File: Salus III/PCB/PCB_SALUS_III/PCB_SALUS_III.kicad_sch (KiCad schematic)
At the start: 42 parts, among them J1 Conn_01x02_Pin, J2 Conn_01x01_Pin, J3 Conn_01x01_Pin, J4 Conn_01x02_Pin, J5 Conn_01x02_Pin, J6 Conn_01x02_Pin, J7 Conn_01x02_Pin, K1 Relay_SPDT, Q1 IRF4905, Q2 IRF4905, Q3 IRF4905, Q4 IRF4905, Q5 IRLB8721PBF, Q6 IRLB8721PBF, Q7 IRLB8721PBF, Q8 IRLB8721PBF, Q9 IRLB8721PBF, U1 ESP32-DEVKITC-32D, U2 RASPBERRY_PI_4B_4GB

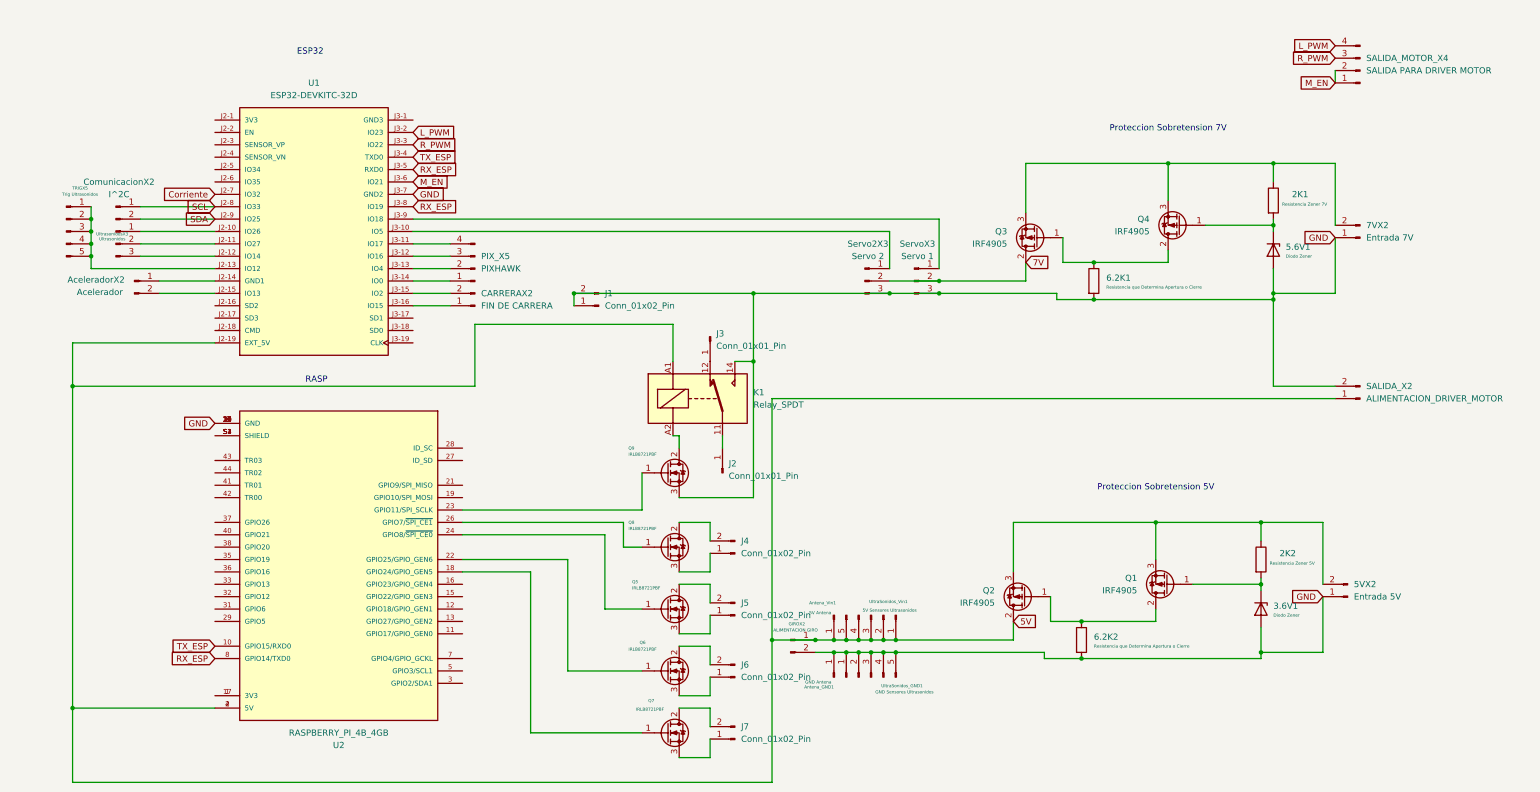
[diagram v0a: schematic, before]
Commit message: Se agregaron Modificaciones de PCB. Queda modificar raspy por tira de pines
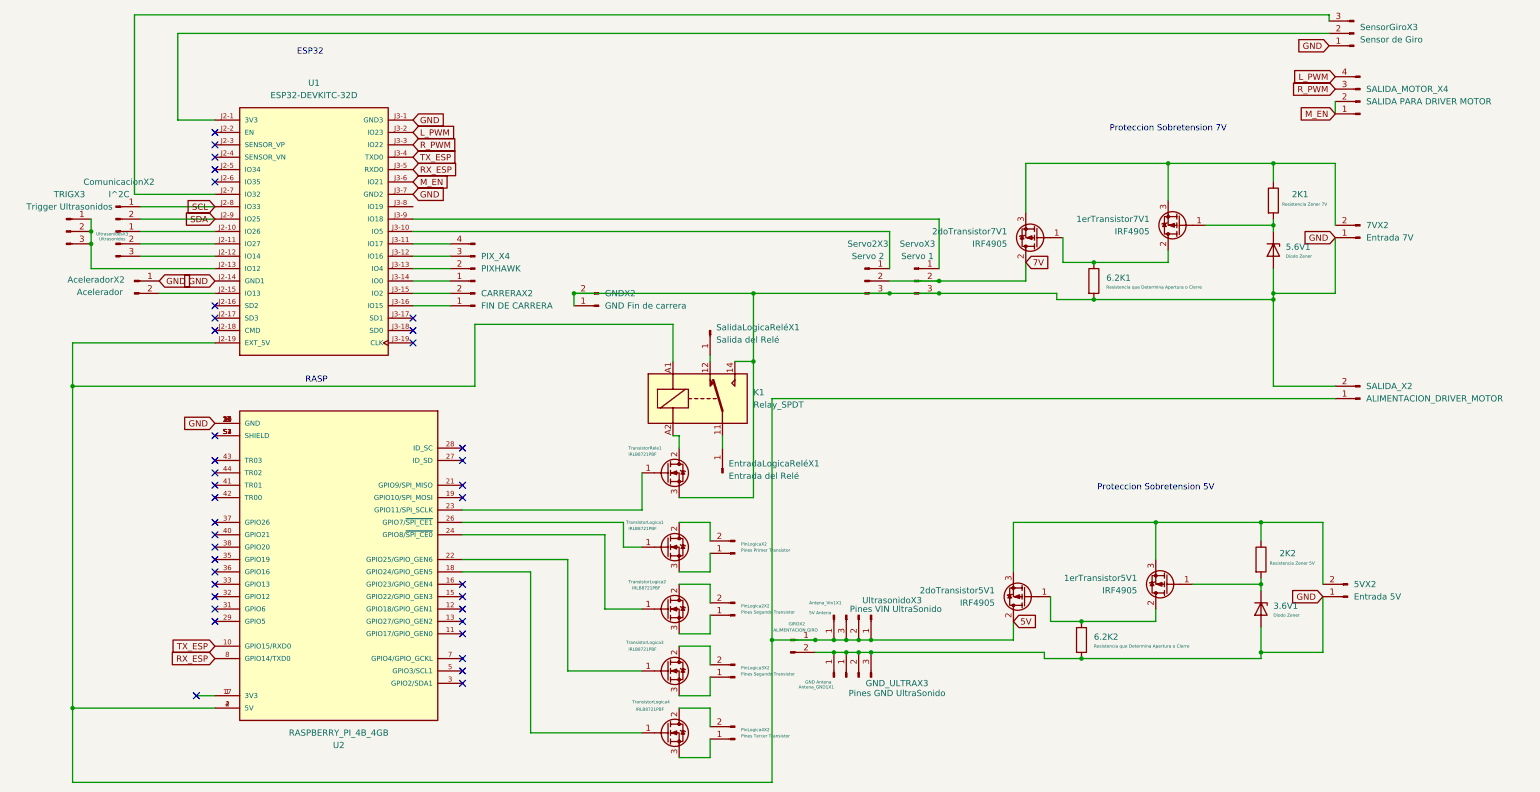
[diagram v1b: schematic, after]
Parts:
- removed TRIGX5: Trig Ultrasonidos, symbol Connector:Conn_01x05_Pin
- removed UltraSonidos_GND1: GND Sensores Ultrasonidos, symbol Connector:Conn_01x05_Pin
- removed UltraSonidos_Vin1: 5V Sensores Ultrasonidos, symbol Connector:Conn_01x05_Pin
- added GND_ULTRAX3: Pines GND UltraSonido, Connector_PinHeader_2.54mm:PinHeader_1x03_P2.54mm_Vertical, symbol Connector:Conn_01x03_Pin
- added SensorGiroX3: Sensor de Giro, Connector_PinHeader_2.54mm:PinHeader_1x03_P2.54mm_Vertical, symbol Connector:Conn_01x03_Pin
- added TRIGX3: Trigger Ultrasonidos, Connector_PinHeader_2.54mm:PinHeader_1x03_P2.54mm_Vertical, symbol Connector:Conn_01x03_Pin
- added UltrasonidoX3: Pines VIN UltraSonido, Connector_PinHeader_2.54mm:PinHeader_1x03_P2.54mm_Vertical, symbol Connector:Conn_01x03_Pin
- 2K1, 2K2, 6.2K1, 6.2K2: footprint (none) -> Resistor_THT:R_Axial_DIN0207_L6.3mm_D2.5mm_P10.16mm_Horizontal
- 3.6V1, 5.6V1: footprint (none) -> Diode_THT:D_DO-41_SOD81_P12.70mm_Horizontal
- 5VX2, 7VX2, AceleradorX2, CARRERAX2, ComunicacionX2, GIROX2, SALIDA_X2: footprint (none) -> Connector_PinHeader_2.54mm:PinHeader_1x02_P2.54mm_Vertical
- Antena_GND1X1: renamed from Antena_GND1; footprint (none) -> Connector_PinHeader_2.54mm:PinHeader_1x01_P2.54mm_Vertical
- Antena_Vin1X1: renamed from Antena_Vin1; footprint (none) -> Connector_PinHeader_2.54mm:PinHeader_1x01_P2.54mm_Vertical
- EntradaLogicaReléX1: renamed from J2; value Conn_01x01_Pin -> Entrada del Relé; footprint (none) -> Connector_PinHeader_2.54mm:PinHeader_1x01_P2.54mm_Vertical
- GNDX2: renamed from J1; value Conn_01x02_Pin -> GND Fin de carrera; footprint (none) -> Connector_PinHeader_2.54mm:PinHeader_1x02_P2.54mm_Vertical
- K1: footprint (none) -> Relay_THT:Relay_SPDT_Finder_36.11
- PIX_X4: renamed from PIX_X5; footprint (none) -> Connector_PinSocket_2.54mm:PinSocket_1x04_P2.54mm_Vertical
- PinLogica2X2: renamed from J5; value Conn_01x02_Pin -> Pines Segundo Transistor; footprint (none) -> Connector_PinHeader_2.54mm:PinHeader_1x02_P2.54mm_Vertical
- PinLogica3X2: renamed from J6; value Conn_01x02_Pin -> Pines Segundo Transistor; footprint (none) -> Connector_PinHeader_2.54mm:PinHeader_1x02_P2.54mm_Vertical
- PinLogica4X2: renamed from J7; value Conn_01x02_Pin -> Pines Tercer Transistor; footprint (none) -> Connector_PinHeader_2.54mm:PinHeader_1x02_P2.54mm_Vertical
- PinLogicaX2: renamed from J4; value Conn_01x02_Pin -> Pines Primer Transistor; footprint (none) -> Connector_PinHeader_2.54mm:PinHeader_1x02_P2.54mm_Vertical
- SALIDA_MOTOR_X4: footprint (none) -> Connector_PinHeader_2.54mm:PinHeader_1x04_P2.54mm_Vertical
- SalidaLogicaReléX1: renamed from J3; value Conn_01x01_Pin -> Salida del Relé; footprint (none) -> Connector_PinHeader_2.54mm:PinHeader_1x01_P2.54mm_Vertical
- Servo2X3, ServoX3, UltrasonidosX3: footprint (none) -> Connector_PinHeader_2.54mm:PinHeader_1x03_P2.54mm_Vertical
- U1: footprint ESP32-DEVKITC-32D:MODULE_ESP32-DEVKITC-32D -> Huella ESP:MODULE_ESP32-DEVKITC-32D
- U2: footprint RASPBERRY_PI_4B_4GB:MODULE_RASPBERRY_PI_4B_4GB -> Huella_Rasp:MODULE_RASPBERRY_PI_4B_4GB
- renumbered Q1 to 1erTransistor5V1, Q4 to 1erTransistor7V1, Q2 to 2doTransistor5V1, Q3 to 2doTransistor7V1, Q8 to TransistorLogica1, Q5 to TransistorLogica2, Q6 to TransistorLogica3, Q7 to TransistorLogica4, Q9 to TransistorRele1
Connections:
- net 5V: now also UltrasonidoX3.1 (Pin_1), UltrasonidoX3.2 (Pin_2), UltrasonidoX3.3 (Pin_3)
- net GND: now also AceleradorX2.1 (Pin_1), U1.J2-14 (GND1), U1.J3-1 (GND3), GND_ULTRAX3.1 (Pin_1), GND_ULTRAX3.2 (Pin_2), GND_ULTRAX3.3 (Pin_3), SensorGiroX3.1 (Pin_1)
- net RX_ESP: no longer U1.J3-8 (IO19)
- net at U1.J2-1 (3V3): now also SensorGiroX3.2 (Pin_2)
- net at U1.J2-13 (IO12): now also TRIGX3.1 (Pin_1), TRIGX3.2 (Pin_2), TRIGX3.3 (Pin_3)
- net Corriente: no longer names the net of U1.J2-7 (IO32)
- net Corriente: now also SensorGiroX3.3 (Pin_3)
- no-connect marks 0 -> 38
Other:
- moved on the sheet: SALIDA_MOTOR_X4, SalidaLogicaReléX1

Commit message: Parece ser la PCB definitiva de SALUS III por lo menos parte logica
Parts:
- removed U2: RASPBERRY_PI_4B_4GB, Huella_Rasp:MODULE_RASPBERRY_PI_4B_4GB, symbol RASPBERRY_PI_4B_4GB:RASPBERRY_PI_4B_4GB
- added 47K1: Resistencia Base 5V, Resistor_THT:R_Axial_DIN0207_L6.3mm_D2.5mm_P10.16mm_Horizontal, symbol Device:R
- added 47K2: Resistencia Base 7V, Resistor_THT:R_Axial_DIN0207_L6.3mm_D2.5mm_P10.16mm_Horizontal, symbol Device:R
- added J1, J2: Conn_01x20_Pin, Connector_PinHeader_2.54mm:PinHeader_1x20_P2.54mm_Vertical, symbol Connector:Conn_01x20_Pin
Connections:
- net 5V: now also J2.1 (Pin_1)
- net GND: now also J1.1 (Pin_1), J1.16 (Pin_16), J2.10 (Pin_10), J2.15 (Pin_15), J2.17 (Pin_17), J2.3 (Pin_3), J2.7 (Pin_7)
- net L_PWM: now also U1.J3-3 (IO22); no longer U1.J3-2 (IO23)
- net RX_ESP: now also J2.5 (Pin_5)
- net R_PWM: now also U1.J3-2 (IO23); no longer U1.J3-3 (IO22)
- net TX_ESP: now also J2.4 (Pin_4)
- net at TransistorLogica1.1 (G): now also J2.11 (Pin_11)
- net at TransistorLogica4.1 (G): now also J2.16 (Pin_16)
- net at TransistorLogica3.1 (G): now also J2.13 (Pin_13)
- net at TransistorRele1.1 (G): now also J2.9 (Pin_9)
- net at TransistorLogica2.1 (G): now also J2.12 (Pin_12)
- net at 2K1.2, 5.6V1.1 (K): now also 47K2.1; no longer 1erTransistor7V1.1 (G)
- net at 2K2.2, 3.6V1.1 (K): now also 47K1.1; no longer 1erTransistor5V1.1 (G)
- new net: 1erTransistor7V1.1 (G), 47K2.2
- new net: 1erTransistor5V1.1 (G), 47K1.2
- no-connect marks 38 -> 36
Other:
- note added: "3V"
- note added: "3V3"
- note added: "5V"
- note added: "GND"
- note added: "Gpio 0"
- note added: "Gpio 1"
- note added: "Gpio 10"
- note added: "Gpio 11"
- note added: "Gpio 12"
- note added: "Gpio 13"
- note added: "Gpio 14 (TX)"
- note added: "Gpio 15 (RX)"
- note added: "Gpio 16"
- note added: "Gpio 17"
- note added: "Gpio 18"
- note added: "Gpio 19"
- note added: "Gpio 2 SDA"
- note added: "Gpio 20"
- note added: "Gpio 21"
- note added: "Gpio 22"
- note added: "Gpio 23"
- note added: "Gpio 24"
- note added: "Gpio 25"
- note added: "Gpio 26"
- note added: "Gpio 27"
- note added: "Gpio 3 SCL"
- note added: "Gpio 4"
- note added: "Gpio 5"
- note added: "Gpio 6"
- note added: "Gpio 7"
- note added: "Gpio 8"
- note added: "Gpio 9"

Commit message: se agrego el diodo TVS a probar para proteger de cierres de Relé
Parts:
- added D1: 1N62xxA, Diode_THT:D_DO-201AE_P15.24mm_Horizontal, symbol Diode:1N62xxA
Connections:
- net GND: now also D1.2 (A2)
- net at K1.A2, TransistorRele1.2 (D): now also D1.1 (A1)
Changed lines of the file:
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@@
 	)
 	(junction
+		(at 139.7 109.22)
+		(diameter 0)
+		(color 0 0 0 0)
+	)
+	(junction
 		(at 173.99 152.4)
 		(diameter 0)
@@
 	(wire
 		(pts
-			(xy 139.7 107.95) (xy 139.7 110.49)
+			(xy 139.7 148.59) (xy 146.05 148.59)
 		)
 		(stroke
@@
 	(wire
 		(pts
-			(xy 139.7 148.59) (xy 146.05 148.59)
+			(xy 44.45 73.66) (xy 19.05 73.66)
 		)
 		(stroke
@@
 	(wire
 		(pts
-			(xy 44.45 73.66) (xy 19.05 73.66)
+			(xy 19.05 68.58) (xy 19.05 73.66)
 		)
 		(stroke
@@
 	(wire
 		(pts
-			(xy 19.05 68.58) (xy 19.05 73.66)
+			(xy 102.87 156.21) (xy 132.08 156.21)
 		)
 		(stroke
@@
 	(wire
 		(pts
-			(xy 102.87 156.21) (xy 132.08 156.21)
+			(xy 69.85 142.24) (xy 102.87 142.24)
 		)
 		(stroke
@@
 	(wire
 		(pts
-			(xy 69.85 142.24) (xy 102.87 142.24)
+			(xy 139.7 107.95) (xy 139.7 109.22)
 		)
 		(stroke
@@
 	(wire
 		(pts
+			(xy 80.01 116.84) (xy 69.85 116.84)
+		)
+		(stroke
+			(width 0)
+			(type default)
+		)
+	)
+	(wire
+		(pts
 			(xy 151.13 92.71) (xy 154.94 92.71)
 		)
@@
 	(wire
 		(pts
+			(xy 80.01 109.22) (xy 80.01 116.84)
+		)
+		(stroke
+			(width 0)
+			(type default)
+		)
+	)
+	(wire
+		(pts
 			(xy 176.53 152.4) (xy 179.07 152.4)
 		)
@@
 	(wire
 		(pts
+			(xy 132.08 109.22) (xy 80.01 109.22)
+		)
+		(stroke
+			(width 0)
+			(type default)
+		)
+	)
+	(wire
+		(pts
 			(xy 261.62 64.77) (xy 261.62 66.04)
 		)
@@
 	(wire
 		(pts
+			(xy 139.7 109.22) (xy 139.7 110.49)
+		)
+		(stroke
+			(width 0)
+			(type default)
+		)
+	)
+	(wire
+		(pts
 			(xy 210.82 62.23) (xy 210.82 52.07)
 		)
@@
 					(unit 1)
 				)
+			)
+		)
+	)
+	(symbol
+		(lib_id "Diode:1N62xxA")
+		(at 135.89 109.22 180)
+		(unit 1)
+		(exclude_from_sim no)
+		(in_bom yes)
+		(on_board yes)
+		(dnp no)
+		(fields_autoplaced yes)
+		(property "Reference" "D1"
+			(at 135.89 102.87 0)
+			(effects
+				(font
+					(size 1.27 1.27)
+				)
+			)
+		)
+		(property "Value" "1N62xxA"
+			(at 135.89 105.41 0)
+			(effects
+				(font
+					(size 1.27 1.27)
+				)
+			)
+		)
+		(property "Footprint" "Diode_THT:D_DO-201AE_P15.24mm_Horizontal"
+			(at 135.89 104.14 0)
+			(effects
+				(font
+					(size 1.27 1.27)
+				)
+				(hide yes)
+			)
+		)
+		(property "Datasheet" "https://www.vishay.com/docs/88301/15ke.pdf"
+			(at 137.16 109.22 0)
+			(effects
+				(font
+					(size 1.27 1.27)
+				)
+				(hide yes)
+			)
+		)
+		(property "Description" "1500W unidirectional TRANSZORB® Transient Voltage Suppressor, DO-201AE"
+			(at 135.89 109.22 0)
+			(effects
+				(font
+					(size 1.27 1.27)
+				)
+				(hide yes)
+			)
+		)
+		(pin "2"
+		)
+		(pin "1"
+		)
+		(instances
+			(project ""
+				(path "/3613b1f1-6164-4a03-ab5f-c520c1df4874"
+					(reference "D1")
+					(unit 1)
+				)

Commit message: Cambios para realizarla en acido preparados
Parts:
- D1: footprint Diode_THT:D_DO-201AE_P15.24mm_Horizontal -> Diode_THT:D_DO-201AE_P12.70mm_Horizontal
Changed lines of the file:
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@@
 			)
 		)
-		(property "Footprint" "Diode_THT:D_DO-201AE_P15.24mm_Horizontal"
+		(property "Footprint" "Diode_THT:D_DO-201AE_P12.70mm_Horizontal"
 			(at 135.89 104.14 0)
 			(effects

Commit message: no se que cambio
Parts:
- removed SensorGiroX3: Sensor de Giro, Connector_PinHeader_2.54mm:PinHeader_1x03_P2.54mm_Vertical, symbol Connector:Conn_01x03_Pin
- added Giro1: Conn_01x02_Pin, Connector_PinHeader_2.54mm:PinHeader_1x02_P2.54mm_Vertical, symbol Connector:Conn_01x02_Pin
- added Pan1, PinesAnalogicos1, SensorCorriente1, Tilt1: Conn_01x03_Pin, Connector_PinHeader_2.54mm:PinHeader_1x03_P2.54mm_Vertical, symbol Connector:Conn_01x03_Pin
- added SensorTemperatura1: Conn_01x04_Pin, Connector_PinHeader_2.54mm:PinHeader_1x04_P2.54mm_Vertical, symbol Connector:Conn_01x04_Pin
- D1: footprint Diode_THT:D_DO-201AE_P12.70mm_Horizontal -> Diode_THT:D_DO-201AE_P15.24mm_Horizontal
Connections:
- net 5V: now also Giro1.2 (Pin_2), Pan1.2 (Pin_2), SensorTemperatura1.4 (Pin_4), Tilt1.2 (Pin_2)
- net GND: now also Giro1.1 (Pin_1), Pan1.1 (Pin_1), SensorCorriente1.1 (Pin_1), SensorTemperatura1.3 (Pin_3), Tilt1.1 (Pin_1)
- net SCL: now also SensorTemperatura1.1 (Pin_1)
- net SDA: now also SensorTemperatura1.2 (Pin_2)
- net at TransistorLogica1.1 (G): now also J2.9 (Pin_9); no longer J2.11 (Pin_11)
- net at U1.J2-1 (3V3): now also SensorCorriente1.2 (Pin_2)
- net at U1.J2-4 (SENSOR_VN): now also PinesAnalogicos1.1 (Pin_1)
- net at U1.J2-5 (IO34): now also PinesAnalogicos1.2 (Pin_2)
- net at U1.J2-6 (IO35): now also PinesAnalogicos1.3 (Pin_3)
- net at U1.J2-7 (IO32): now also SensorCorriente1.3 (Pin_3)
- net at TransistorLogica4.1 (G): now also J1.2 (Pin_2); no longer J2.16 (Pin_16)
- net at TransistorLogica2.1 (G): now also J2.11 (Pin_11); no longer J2.12 (Pin_12)
- net at TransistorLogica3.1 (G): now also J2.18 (Pin_18); no longer J2.13 (Pin_13)
- net at TransistorRele1.1 (G): now also J2.8 (Pin_8); no longer J2.9 (Pin_9)
- net at J2.6 (Pin_6): now also Tilt1.3 (Pin_3)
- new net: J2.16 (Pin_16), Pan1.3 (Pin_3)
- no-connect marks 36 -> 31
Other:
- note added: "En el diagrama de circuito esta dada vuelta la tira de pinas, eso hay que cambiarlo Y agregar un Pin mas de 5V para que le de la corriente a la Rasp"
